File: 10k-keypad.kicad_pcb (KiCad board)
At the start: 2 copper layers, 42 parts, among them J1 AVR-ISP-6, K1 SW_Push, K10 SW_Push, K2 SW_Push, K3 SW_Push, K4 SW_Push, K5 SW_Push, K6 SW_Push, K7 SW_Push, K8 SW_Push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

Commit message: crystal clock
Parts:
- moved F1 143.2 mm to (138.4, 22.4)
- moved Y1 121.2 mm to (146.3, 41.1), turned to -90 degrees
- moved C3 96.9 mm to (142.0, 42.7), turned to 180 degrees
- moved C2 96.9 mm to (142.0, 39.6), turned to 180 degrees
- moved C8 91.8 mm to (147.3, 45.7), turned to 90 degrees
- moved D10 19.0 mm to (169.9, 56.9)
- moved D11 19.0 mm to (150.9, 56.9)
- moved C1 7.34 mm to (244.6, 27.7)
- moved D6 3.17 mm to (135.1, 39.9)
- moved USB1 0.58 mm to (154.2, 15.1)
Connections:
- U1 pad 5: COL5 -> unconnected-(U1-PC2-Pad5)
- U1 pad 8: unconnected-(U1-PD2-Pad8) -> COL5
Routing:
- net ROW1: track 0.00 -> 123.7 mm, vias 0 -> 5
- net ROW2: track 0.00 -> 76.2 mm
- net COL5: track 0.00 -> 34.0 mm
- net COL4: track 0.00 -> 26.4 mm
- net GND: track 0.00 -> 24.2 mm
- net COL1: track 0.00 -> 20.9 mm
- net Net-(D6-A): track 0.00 -> 20.7 mm, vias 0 -> 1
- net COL2: track 0.00 -> 19.5 mm
- net COL3: track 0.00 -> 19.2 mm
- net XTAL2: track 0.00 -> 9.88 mm
- net XTAL1: track 0.00 -> 9.09 mm
- net +5V: track 0.00 -> 6.22 mm
- net Net-(D3-A): track 0.00 -> 2.78 mm
- net Net-(D8-A): track 0.00 -> 2.78 mm
- net Net-(D5-A): track 0.00 -> 2.78 mm
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
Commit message: finish routing
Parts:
- removed C5, C6, C7: 0.1u, Capacitor_SMD:C_0805_2012Metric_Pad1.18x1.45mm_HandSolder
- moved R5 99.9 mm to (148.8, 26.4), turned to 180 degrees
- moved C4 93.3 mm to (146.1, 30.7)
- moved R6 92.3 mm to (160.3, 26.4)
- moved FB1 82.4 mm to (162.6, 22.9)
- moved R3 82.2 mm to (153.9, 51.8), turned to -90 degrees
- moved C1 79.2 mm to (166.1, 38.1), turned to 180 degrees
- moved R4 46.0 mm to (200.4, 45.0)
- moved F1 7.89 mm to (145.0, 26.7), turned to -90 degrees
- moved R1 0.57 mm to (154.9, 35.3)
- moved R2 0.57 mm to (152.9, 35.3)
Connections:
- U1 pad 10: unconnected-(U1-PD4-Pad10) -> ROW2
- U1 pad 20: unconnected-(U1-PB6-Pad20) -> COL4
- U1 pad 21: unconnected-(U1-PB7-Pad21) -> COL3
- U1 pad 22: COL4 -> COL2
- U1 pad 23: COL3 -> COL1
- U1 pad 25: COL2 -> unconnected-(U1-PC5-Pad25)
- U1 pad 26: COL1 -> unconnected-(U1-PC4-Pad26)
- U1 pad 6: ROW2 -> unconnected-(U1-PD0-Pad6)
- U1 pad 7: ROW1 -> unconnected-(U1-PD1-Pad7)
- U1 pad 9: unconnected-(U1-PD3-Pad9) -> ROW1
- USB1 pad 13: GND -> Earth
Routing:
- net GND: track 24.2 -> 218.4 mm, vias 0 -> 10
- net +5V: track 6.22 -> 148.3 mm, vias 0 -> 7
- net RESET: track 0.00 -> 65.1 mm, vias 0 -> 5
- net COL1: track 20.9 -> 81.5 mm, vias 0 -> 4
- net SCK: track 0.00 -> 39.4 mm, vias 0 -> 3
- net MOSI: track 0.00 -> 38.9 mm, vias 0 -> 3
- net COL2: track 19.5 -> 56.2 mm, vias 0 -> 4
- net MISO: track 0.00 -> 32.7 mm, vias 0 -> 3
- net Earth: track 0.00 -> 30.5 mm
- net COL3: track 19.2 -> 38.5 mm, vias 0 -> 2
- net VCC: track 0.00 -> 18.7 mm, vias 0 -> 3
- net Net-(U1-UCAP): track 0.00 -> 13.5 mm, vias 0 -> 2
- net ROW2: track 76.2 -> 87.5 mm
- net Net-(USB1-CC1): track 0.00 -> 6.05 mm
- net Net-(USB1-CC2): track 0.00 -> 4.94 mm
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- added copper zone on B.Cu, net Earth
- added copper zone on F.Cu, net Earth
- added copper zone on B.Cu, net GND
- added copper zone on F.Cu, net GND

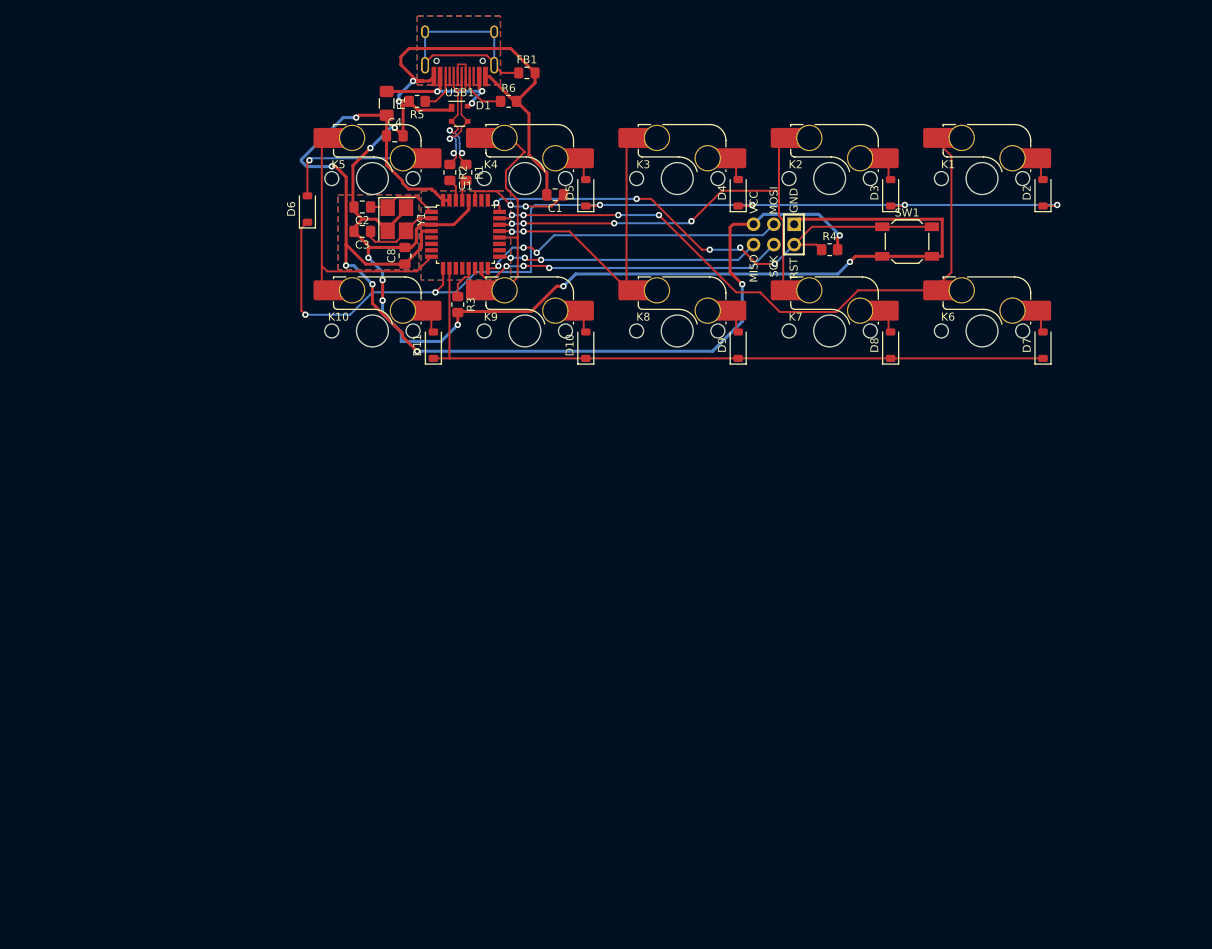
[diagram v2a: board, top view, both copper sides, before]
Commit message: board cutout
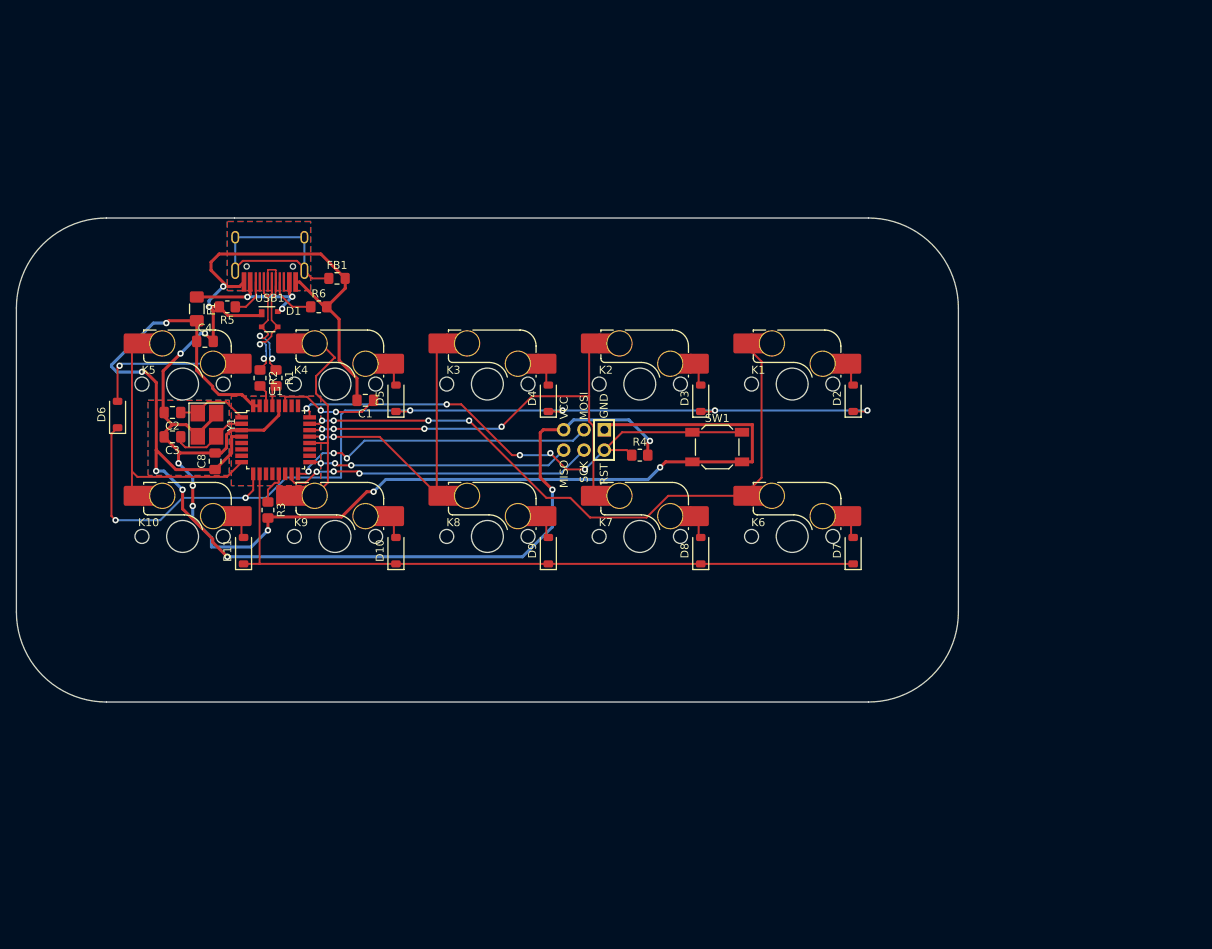
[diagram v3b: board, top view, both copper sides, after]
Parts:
- moved C4 35.0 mm to (122.3, 56.4)
- moved C1 35.0 mm to (142.4, 63.8)
- moved D11 35.0 mm to (127.1, 82.6)
- moved D2 35.0 mm to (203.3, 63.5)
- moved D3 35.0 mm to (184.3, 63.5)
- moved D4 35.0 mm to (165.2, 63.5)
- moved D7 35.0 mm to (203.3, 82.6)
- moved D8 35.0 mm to (184.3, 82.6)
- moved D9 35.0 mm to (165.2, 82.6)
- moved FB1 35.0 mm to (138.8, 48.5)
- moved J1 35.0 mm to (169.7, 68.7)
- moved K10 35.0 mm to (119.5, 80.8)
- moved K2 35.0 mm to (176.7, 61.8)
- moved K3 35.0 mm to (157.6, 61.8)
- moved K4 35.0 mm to (138.6, 61.8)
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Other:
- board outline added: 117.8 x 60.5 mm

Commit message: clearance fix
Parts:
- moved C4 4.99 mm to (126.9, 54.5), turned to 180 degrees
- moved C8 0.27 mm to (123.4, 71.6)
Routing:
- net +5V: track 148.3 -> 155.8 mm
- net COL5: track 34.0 -> 32.5 mm

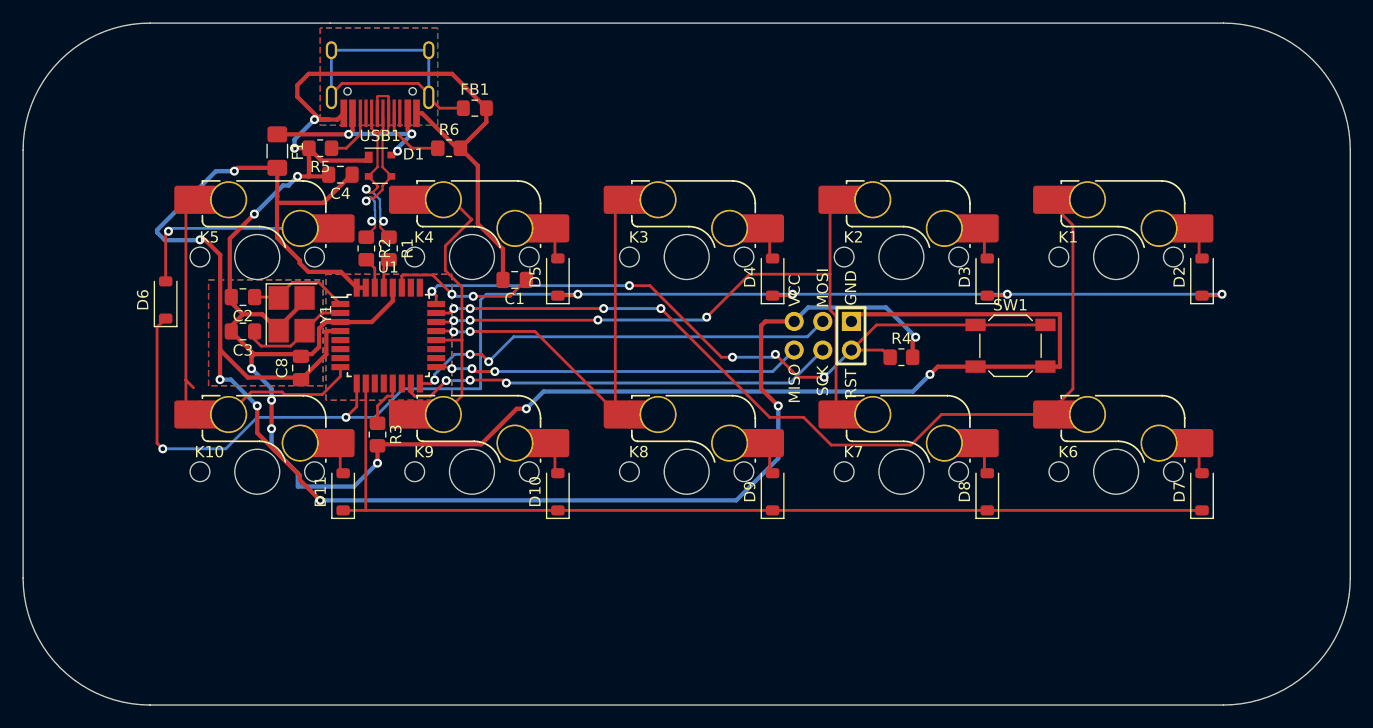
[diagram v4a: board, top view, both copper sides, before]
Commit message: fix edge cut
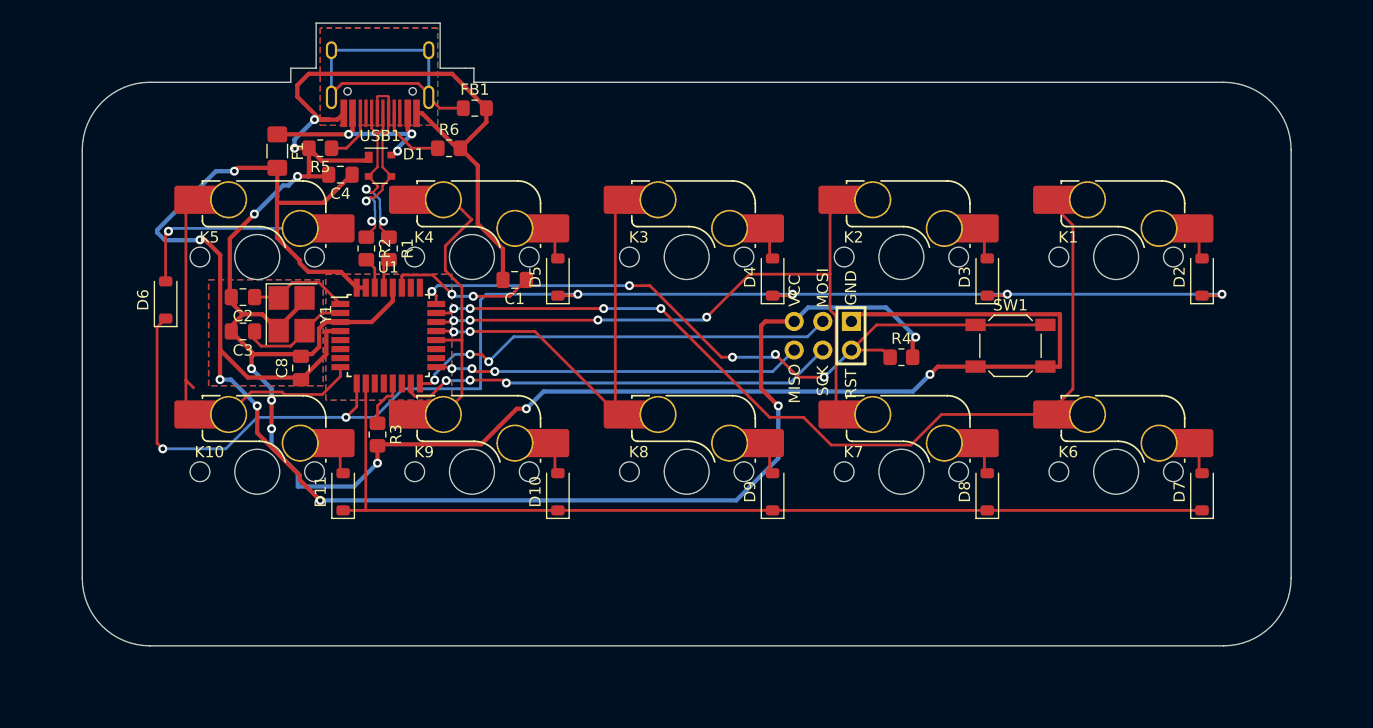
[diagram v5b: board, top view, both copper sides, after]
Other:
- board size 117.8 x 60.5 mm -> 107.2 x 55.2 mm

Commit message: hall sensor circuitry
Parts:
- added C10: 100n, Capacitor_SMD:C_0805_2012Metric_Pad1.18x1.45mm_HandSolder, F.Cu at (150.8, 78.5)
- added C11: 4.7n, Capacitor_SMD:C_0805_2012Metric_Pad1.18x1.45mm_HandSolder, F.Cu at (153.2, 85.5)
- added C12: 100n, Capacitor_SMD:C_0805_2012Metric_Pad1.18x1.45mm_HandSolder, F.Cu at (133.0, 83.2)
- added C13: 4.7n, Capacitor_SMD:C_0805_2012Metric_Pad1.18x1.45mm_HandSolder, F.Cu at (134.2, 85.5)
- added C14: 100n, Capacitor_SMD:C_0805_2012Metric_Pad1.18x1.45mm_HandSolder, F.Cu at (112.5, 79.8)
- added C15: 4.7n, Capacitor_SMD:C_0805_2012Metric_Pad1.18x1.45mm_HandSolder, F.Cu at (115.2, 85.5)
- added C5: 4.7n, Capacitor_SMD:C_0805_2012Metric_Pad1.18x1.45mm_HandSolder, F.Cu at (191.2, 85.8)
- added C6: 100n, Capacitor_SMD:C_0805_2012Metric_Pad1.18x1.45mm_HandSolder, F.Cu at (188.8, 78.5)
- added C7: 100n, Capacitor_SMD:C_0805_2012Metric_Pad1.18x1.45mm_HandSolder, F.Cu at (168.5, 79.2)
- added C9: 4.7n, Capacitor_SMD:C_0805_2012Metric_Pad1.18x1.45mm_HandSolder, F.Cu at (172.2, 85.8)
- added D12: D, Diode_SMD:D_SOD-123, F.Cu at (199.8, 85.5)
- added D13: D, Diode_SMD:D_SOD-123, F.Cu at (180.8, 85.5)
- added D14: D, Diode_SMD:D_SOD-123, F.Cu at (161.5, 85.5)
- added D15: D, Diode_SMD:D_SOD-123, F.Cu at (142.5, 85.5)
- added D16: D, Diode_SMD:D_SOD-123, F.Cu at (123.5, 85.5)
- added U2: DRV5055A2xDBZxQ1, Package_TO_SOT_SMD:SOT-23, F.Cu at (195.7, 80.8)
- added U3: DRV5055A2xDBZxQ1, Package_TO_SOT_SMD:SOT-23, F.Cu at (176.7, 80.8)
- added U4: DRV5055A2xDBZxQ1, Package_TO_SOT_SMD:SOT-23, F.Cu at (157.6, 80.8)
- added U5: DRV5055A2xDBZxQ1, Package_TO_SOT_SMD:SOT-23, F.Cu at (138.6, 80.8)
- added U6: DRV5055A2xDBZxQ1, Package_TO_SOT_SMD:SOT-23, F.Cu at (119.5, 80.8)
- K10, K6, K7, K8, K9: footprint marbastlib-mx:SW_MX_HS_CPG151101S11_1u -> Hall:SW_MX_HS_CPG151101S11_1u_no_center_piece
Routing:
- net GND: track 218.7 -> 396.7 mm
- net ROW2: track 87.5 -> 106.4 mm, vias 0 -> 5
- net Net-(D16-A): track 0.00 -> 14.0 mm, vias 0 -> 2
- net COL4: track 28.7 -> 40.4 mm, vias 0 -> 2
- net COL2: track 56.2 -> 67.6 mm, vias 4 -> 6
- net Net-(D13-A): track 0.00 -> 10.6 mm
- net Net-(D12-A): track 0.00 -> 10.4 mm
- net COL5: track 32.5 -> 42.8 mm
- net Net-(D14-A): track 0.00 -> 10.0 mm
- net Net-(D15-A): track 0.00 -> 9.89 mm
- net COL1: track 81.5 -> 90.7 mm
- net COL3: track 38.5 -> 47.6 mm
- net D-: track 18.8 -> 17.5 mm
- net D+: track 16.9 -> 15.8 mm

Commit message: narrower edges, fill fix
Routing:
- net GND: vias 10 -> 13
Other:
- board size 107.2 x 55.2 mm -> 103.2 x 53.2 mm
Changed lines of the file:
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@@
     )
   )
-  (gr_line (start 211.25 52.25) (end 211.25 90.25)
-    (stroke (width 0.1) (type default)) (layer "Edge.Cuts"))
-  (gr_arc (start 211.25 90.25) (mid 209.492641 94.492641) (end 205.25 96.25)
-    (stroke (width 0.1) (type default)) (layer "Edge.Cuts"))
-  (gr_line (start 124.75 41) (end 135.75 41)
-    (stroke (width 0.1) (type default)) (layer "Edge.Cuts"))
-  (gr_line (start 122.5 45) (end 124.75 45)
-    (stroke (width 0.1) (type default)) (layer "Edge.Cuts"))
-  (gr_line (start 138 45) (end 138.75 45)
-    (stroke (width 0.1) (type default)) (layer "Edge.Cuts"))
-  (gr_line (start 138.75 45) (end 138.75 46.25)
-    (stroke (width 0.1) (type default)) (layer "Edge.Cuts"))
-  (gr_line (start 104 52.25) (end 104 90.25)
-    (stroke (width 0.1) (type default)) (layer "Edge.Cuts"))
-  (gr_line (start 205.25 96.25) (end 110 96.25)
-    (stroke (width 0.1) (type default)) (layer "Edge.Cuts"))
-  (gr_arc (start 110 96.25) (mid 105.757359 94.492641) (end 104 90.25)
-    (stroke (width 0.1) (type default)) (layer "Edge.Cuts"))
-  (gr_arc (start 205.25 46.25) (mid 209.492641 48.007359) (end 211.25 52.25)
-    (stroke (width 0.1) (type default)) (layer "Edge.Cuts"))
-  (gr_line (start 135.75 45) (end 138 45)
-    (stroke (width 0.1) (type default)) (layer "Edge.Cuts"))
-  (gr_arc (start 104 52.25) (mid 105.757359 48.007359) (end 110 46.25)
-    (stroke (width 0.1) (type default)) (layer "Edge.Cuts"))
-  (gr_line (start 122.5 46.25) (end 110 46.25)
-    (stroke (width 0.1) (type default)) (layer "Edge.Cuts"))
-  (gr_line (start 122.5 46.25) (end 122.5 45)
-    (stroke (width 0.1) (type default)) (layer "Edge.Cuts"))
-  (gr_line (start 124.75 45) (end 124.75 41)
-    (stroke (width 0.1) (type default)) (layer "Edge.Cuts"))
-  (gr_line (start 135.75 41) (end 135.75 45)
-    (stroke (width 0.1) (type default)) (layer "Edge.Cuts"))
-  (gr_line (start 138.75 46.25) (end 205.25 46.25)
+  (gr_line (start 209.25 52.25) (end 209.25 90.25)
+    (stroke (width 0.1) (type default)) (layer "Edge.Cuts"))
+  (gr_arc (start 209.25 90.25) (mid 208.078427 93.078427) (end 205.25 94.25)
+    (stroke (width 0.1) (type default)) (layer "Edge.Cuts"))
+  (gr_line (start 125.25 41) (end 135.5 41)
+    (stroke (width 0.1) (type default)) (layer "Edge.Cuts"))
+  (gr_arc (start 121 46.25) (mid 121.732233 44.482233) (end 123.5 43.75)
+    (stroke (width 0.1) (type default)) (layer "Edge.Cuts"))
+  (gr_line (start 106 52.25) (end 106 90.25)
+    (stroke (width 0.1) (type default)) (layer "Edge.Cuts"))
+  (gr_line (start 205.25 94.25) (end 110 94.25)
+    (stroke (width 0.1) (type default)) (layer "Edge.Cuts"))
+  (gr_arc (start 110 94.25) (mid 107.171573 93.078427) (end 106 90.25)
+    (stroke (width 0.1) (type default)) (layer "Edge.Cuts"))
+  (gr_line (start 121 46.25) (end 121 48.25)
+    (stroke (width 0.1) (type default)) (layer "Edge.Cuts"))
+  (gr_arc (start 205.25 48.25) (mid 208.078427 49.421573) (end 209.25 52.25)
+    (stroke (width 0.1) (type default)) (layer "Edge.Cuts"))
+  (gr_arc (start 106 52.25) (mid 107.171573 49.421573) (end 110 48.25)
+    (stroke (width 0.1) (type default)) (layer "Edge.Cuts"))
+  (gr_line (start 121 48.25) (end 110 48.25)
+    (stroke (width 0.1) (type default)) (layer "Edge.Cuts"))
+  (gr_line (start 123.5 43.75) (end 125.25 43.75)
+    (stroke (width 0.1) (type default)) (layer "Edge.Cuts"))
+  (gr_line (start 125.25 43.75) (end 125.25 41)
+    (stroke (width 0.1) (type default)) (layer "Edge.Cuts"))
+  (gr_line (start 135.5 41) (end 135.5 43.75)
+    (stroke (width 0.1) (type default)) (layer "Edge.Cuts"))
+  (gr_arc (start 139.25 43.75) (mid 141.017767 44.482233) (end 141.75 46.25)
+    (stroke (width 0.1) (type default)) (layer "Edge.Cuts"))
+  (gr_line (start 141.75 46.25) (end 141.75 48.25)
+    (stroke (width 0.1) (type default)) (layer "Edge.Cuts"))
+  (gr_line (start 141.75 48.25) (end 205.25 48.25)
+    (stroke (width 0.1) (type default)) (layer "Edge.Cuts"))
+  (gr_line (start 139.25 43.75) (end 135.5 43.75)
     (stroke (width 0.1) (type default)) (layer "Edge.Cuts"))
   (segment (start 132.350768 63.421768) (end 132.350768 64.471768) (width 0.25) (layer "F.Cu") (net 1))
@@
   (via (at 123.1 54.6) (size 0.8) (drill 0.4) (layers "F.Cu" "B.Cu") (net 2))
   (via (at 119.269968 57.943968) (size 0.8) (drill 0.4) (layers "F.Cu" "B.Cu") (net 2))
+  (via (at 133.25 66.75) (size 0.8) (drill 0.4) (layers "F.Cu" "B.Cu") (free) (net 2))
   (via (at 124.603968 49.561968) (size 0.8) (drill 0.4) (layers "F.Cu" "B.Cu") (net 2))
   (via (at 120.793968 76.993968) (size 0.8) (drill 0.4) (layers "F.Cu" "B.Cu") (net 2))
   (via (at 130.191968 80.041968) (size 0.8) (drill 0.4) (layers "F.Cu" "B.Cu") (net 2))
+  (via (at 122.25 63) (size 0.8) (drill 0.4) (layers "F.Cu" "B.Cu") (free) (net 2))
+  (via (at 129 70.75) (size 0.8) (drill 0.4) (layers "F.Cu" "B.Cu") (free) (net 2))
   (segment (start 177.698468 73.683468) (end 179.213968 72.167968) (width 0.381) (layer "B.Cu") (net 2))
   (segment (start 122.317968 55.403968) (end 122.317968 55.382032) (width 0.381) (layer "B.Cu") (net 2))
@@
   (segment (start 113.25 84.25) (end 119 84.25) (width 0.25) (layer "B.Cu") (net 52))
   (zone (net 2) (net_name "GND") (layers "F&B.Cu") (hatch edge 0.5)
-    (connect_pads (clearance 0.5))
-    (min_thickness 0.25) (filled_areas_thickness no)
-    (fill yes (thermal_gap 0.5) (thermal_bridge_width 0.5))
-    (polygon
-      (pts
-        (xy 136.795968 74.453968)
-        (xy 125.619968 74.453968)
-        (xy 125.619968 63.277968)
-        (xy 136.795968 63.277968)
-      )
-    )
-  )
-  (zone (net 2) (net_name "GND") (layers "F&B.Cu") (hatch edge 0.5)
     (priority 1)
     (connect_pads (clearance 0.5))
@@
     (polygon
       (pts
-        (xy 125.365968 63.785968)
+        (xy 125.365968 62.25)
         (xy 125.365968 73.183968)
         (xy 115.205968 73.183968)
-        (xy 115.205968 63.785968)
+        (xy 115.205968 62.25)
+      )
+    )
+  )
+  (zone (net 2) (net_name "GND") (layers "F&B.Cu") (hatch edge 0.5)
+    (connect_pads (clearance 0.5))
+    (min_thickness 0.25) (filled_areas_thickness no)
+    (fill yes (thermal_gap 0.5) (thermal_bridge_width 0.5))
+    (polygon
+      (pts
+        (xy 125.75 74.25)
+        (xy 136.5 74.25)
+        (xy 136.5 63.25)
+        (xy 125.75 63.25)
       )
     )
@@
     (polygon
       (pts
-        (xy 125.111968 41.433968)
-        (xy 125.111968 50.069968)
-        (xy 135.525968 50.069968)
-        (xy 135.525968 41.433968)
+        (xy 125.75 41.5)
+        (xy 125.75 45.25)
+        (xy 125.111968 45.25)
+        (xy 125.111968 50.319968)
+        (xy 135.525968 50.319968)
+        (xy 135.5 45.25)
+        (xy 135 45.25)
+        (xy 135 41.5)
       )
     )
